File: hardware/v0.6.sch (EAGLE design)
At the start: 31 parts, among them J2 MAGJACK, U1 ATMEGA168P, U2 ENC28J60, Y1 CRYSTAL-GROUNDED

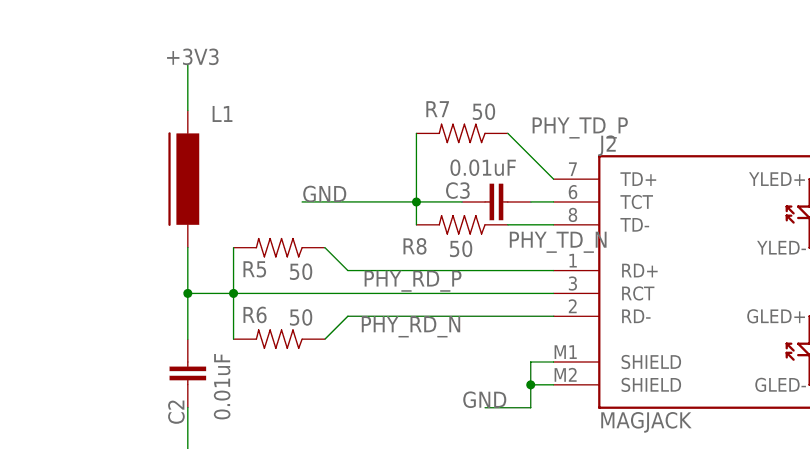
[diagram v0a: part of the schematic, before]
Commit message: Fixed tx diff pair impedence matching (hardware)
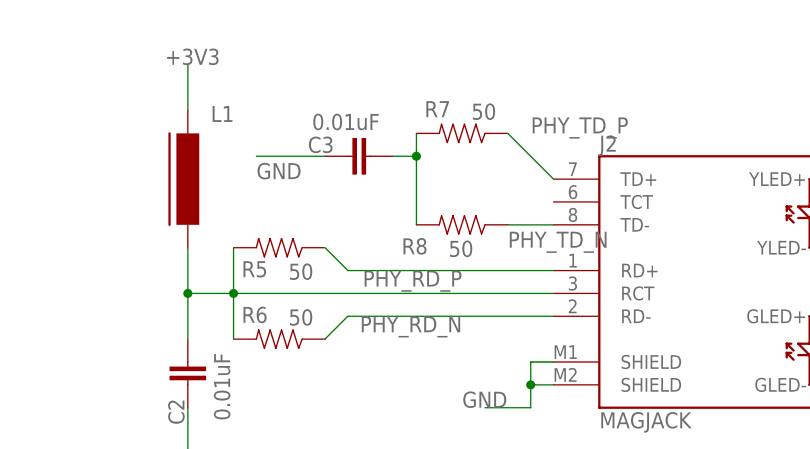
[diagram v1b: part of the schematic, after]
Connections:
- removed net N$5: C3.2, J2.TCT
- new net TDCAP: C3.2, R7.2, R8.2
- net GND: no longer R7.2, R8.2
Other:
- moved on the sheet: C3
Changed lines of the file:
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@@
 <grid distance="0.1" unitdist="inch" unit="inch" style="lines" multiple="1" display="no" altdistance="0.01" altunitdist="inch" altunit="inch"/>
 <layers>
-<layer number="1" name="Top" color="4" fill="1" visible="yes" active="no"/>
-<layer number="16" name="Bottom" color="1" fill="1" visible="yes" active="no"/>
-<layer number="17" name="Pads" color="2" fill="1" visible="yes" active="no"/>
-<layer number="18" name="Vias" color="2" fill="1" visible="yes" active="no"/>
-<layer number="19" name="Unrouted" color="6" fill="1" visible="yes" active="no"/>
-<layer number="20" name="Dimension" color="15" fill="1" visible="yes" active="no"/>
-<layer number="21" name="tPlace" color="7" fill="1" visible="yes" active="no"/>
-<layer number="22" name="bPlace" color="7" fill="1" visible="yes" active="no"/>
-<layer number="23" name="tOrigins" color="15" fill="1" visible="yes" active="no"/>
-<layer number="24" name="bOrigins" color="15" fill="1" visible="yes" active="no"/>
-<layer number="25" name="tNames" color="7" fill="1" visible="yes" active="no"/>
-<layer number="26" name="bNames" color="7" fill="1" visible="yes" active="no"/>
-<layer number="27" name="tValues" color="7" fill="1" visible="yes" active="no"/>
-<layer number="28" name="bValues" color="7" fill="1" visible="yes" active="no"/>
+<layer number="1" name="Top" color="4" fill="1" visible="no" active="no"/>
+<layer number="16" name="Bottom" color="1" fill="1" visible="no" active="no"/>
+<layer number="17" name="Pads" color="2" fill="1" visible="no" active="no"/>
+<layer number="18" name="Vias" color="2" fill="1" visible="no" active="no"/>
+<layer number="19" name="Unrouted" color="6" fill="1" visible="no" active="no"/>
+<layer number="20" name="Dimension" color="15" fill="1" visible="no" active="no"/>
+<layer number="21" name="tPlace" color="7" fill="1" visible="no" active="no"/>
+<layer number="22" name="bPlace" color="7" fill="1" visible="no" active="no"/>
+<layer number="23" name="tOrigins" color="15" fill="1" visible="no" active="no"/>
+<layer number="24" name="bOrigins" color="15" fill="1" visible="no" active="no"/>
+<layer number="25" name="tNames" color="7" fill="1" visible="no" active="no"/>
+<layer number="26" name="bNames" color="7" fill="1" visible="no" active="no"/>
+<layer number="27" name="tValues" color="7" fill="1" visible="no" active="no"/>
+<layer number="28" name="bValues" color="7" fill="1" visible="no" active="no"/>
 <layer number="29" name="tStop" color="7" fill="3" visible="no" active="no"/>
 <layer number="30" name="bStop" color="7" fill="6" visible="no" active="no"/>
@@
 <layer number="35" name="tGlue" color="7" fill="4" visible="no" active="no"/>
 <layer number="36" name="bGlue" color="7" fill="5" visible="no" active="no"/>
-<layer number="37" name="tTest" color="7" fill="1" visible="yes" active="no"/>
-<layer number="38" name="bTest" color="7" fill="1" visible="yes" active="no"/>
+<layer number="37" name="tTest" color="7" fill="1" visible="no" active="no"/>
+<layer number="38" name="bTest" color="7" fill="1" visible="no" active="no"/>
 <layer number="39" name="tKeepout" color="4" fill="11" visible="no" active="no"/>
 <layer number="40" name="bKeepout" color="1" fill="11" visible="no" active="no"/>
@@
 <layer number="44" name="Drills" color="7" fill="1" visible="no" active="no"/>
 <layer number="45" name="Holes" color="7" fill="1" visible="no" active="no"/>
-<layer number="46" name="Milling" color="3" fill="1" visible="yes" active="no"/>
-<layer number="47" name="Measures" color="7" fill="1" visible="yes" active="no"/>
-<layer number="48" name="Document" color="7" fill="1" visible="yes" active="no"/>
-<layer number="49" name="Reference" color="7" fill="1" visible="yes" active="no"/>
-<layer number="50" name="dxf" color="7" fill="1" visible="yes" active="no"/>
-<layer number="51" name="wire" color="7" fill="1" visible="yes" active="no"/>
-<layer number="52" name="bDocu" color="7" fill="1" visible="yes" active="no"/>
-<layer number="53" name="tGND_GNDA" color="7" fill="1" visible="yes" active="no"/>
-<layer number="54" name="bGND_GNDA" color="7" fill="1" visible="yes" active="no"/>
-<layer number="56" name="wert" color="7" fill="1" visible="yes" active="no"/>
-<layer number="57" name="tCAD" color="7" fill="1" visible="yes" active="no"/>
+<layer number="46" name="Milling" color="3" fill="1" visible="no" active="no"/>
+<layer number="47" name="Measures" color="7" fill="1" visible="no" active="no"/>
+<layer number="48" name="Document" color="7" fill="1" visible="no" active="no"/>
+<layer number="49" name="Reference" color="7" fill="1" visible="no" active="no"/>
+<layer number="50" name="dxf" color="7" fill="1" visible="no" active="no"/>
+<layer number="51" name="wire" color="7" fill="1" visible="no" active="no"/>
+<layer number="52" name="bDocu" color="7" fill="1" visible="no" active="no"/>
+<layer number="53" name="tGND_GNDA" color="7" fill="1" visible="no" active="no"/>
+<layer number="54" name="bGND_GNDA" color="7" fill="1" visible="no" active="no"/>
+<layer number="56" name="wert" color="7" fill="1" visible="no" active="no"/>
+<layer number="57" name="tCAD" color="7" fill="1" visible="no" active="no"/>
 <layer number="91" name="Nets" color="2" fill="1" visible="yes" active="yes"/>
 <layer number="92" name="Busses" color="1" fill="1" visible="yes" active="yes"/>
@@
 <attribute name="VALUE" x="114.681" y="6.096" size="1.778" layer="96" rot="R270"/>
 </instance>
-<instance part="C3" gate="G$1" x="147.32" y="22.86" smashed="yes" rot="R90">
-<attribute name="NAME" x="143.256" y="25.019" size="1.778" layer="95" rot="R180"/>
-<attribute name="VALUE" x="148.336" y="27.559" size="1.778" layer="96" rot="R180"/>
+<instance part="C3" gate="G$1" x="132.08" y="27.94" smashed="yes" rot="R90">
+<attribute name="NAME" x="128.016" y="30.099" size="1.778" layer="95" rot="R180"/>
+<attribute name="VALUE" x="133.096" y="32.639" size="1.778" layer="96" rot="R180"/>
 </instance>
 <instance part="R7" gate="G$1" x="142.24" y="30.48" smashed="yes" rot="R180">
@@
 </segment>
 <segment>
-<pinref part="C3" gate="G$1" pin="1"/>
-<wire x1="142.24" y1="22.86" x2="137.16" y2="22.86" width="0.1524" layer="91"/>
-<pinref part="R7" gate="G$1" pin="2"/>
-<wire x1="137.16" y1="22.86" x2="137.16" y2="30.48" width="0.1524" layer="91"/>
-<pinref part="R8" gate="G$1" pin="2"/>
-<wire x1="137.16" y1="22.86" x2="137.16" y2="20.32" width="0.1524" layer="91"/>
-<junction x="137.16" y="22.86"/>
-<wire x1="137.16" y1="22.86" x2="124.46" y2="22.86" width="0.1524" layer="91"/>
-<label x="124.46" y="22.86" size="1.778" layer="95"/>
-</segment>
-<segment>
 <pinref part="J2" gate="G$1" pin="SHIELD@0"/>
 <wire x1="152.4" y1="5.08" x2="149.86" y2="5.08" width="0.1524" layer="91"/>
@@
 <wire x1="175.26" y1="-68.58" x2="175.26" y2="-76.2" width="0.1524" layer="91"/>
 <junction x="175.26" y="-76.2"/>
+</segment>
+<segment>
+<pinref part="C3" gate="G$1" pin="1"/>
+<wire x1="127" y1="27.94" x2="119.38" y2="27.94" width="0.1524" layer="91"/>
+<label x="119.38" y="25.4" size="1.778" layer="95"/>
 </segment>
 </net>
@@
 </segment>
 </net>
-<net name="N$5" class="0">
-<segment>
-<pinref part="C3" gate="G$1" pin="2"/>
-<pinref part="J2" gate="G$1" pin="TCT"/>
-<wire x1="149.86" y1="22.86" x2="152.4" y2="22.86" width="0.1524" layer="91"/>
-</segment>
-</net>
 <net name="PHY_RD_P" class="0">
 <segment>
@@
 </segment>
 </net>
+<net name="TDCAP" class="0">
+<segment>
+<pinref part="R7" gate="G$1" pin="2"/>
+<wire x1="137.16" y1="20.32" x2="137.16" y2="27.94" width="0.1524" layer="91"/>
+<pinref part="R8" gate="G$1" pin="2"/>
+<pinref part="C3" gate="G$1" pin="2"/>
+<wire x1="137.16" y1="27.94" x2="137.16" y2="30.48" width="0.1524" layer="91"/>
+<wire x1="137.16" y1="27.94" x2="134.62" y2="27.94" width="0.1524" layer="91"/>
+<junction x="137.16" y="27.94"/>
+</segment>
+</net>
